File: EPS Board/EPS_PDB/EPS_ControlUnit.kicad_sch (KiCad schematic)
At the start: 42 parts, among them J6 Conn_01x04_Pin, J7 USB_B_Micro, SW1 SW_SPDT, U1 AMS1117-3.3, U2 TPS3824-33QDBVRQ1, U3 STM32L476VET6, Y1 32MHz

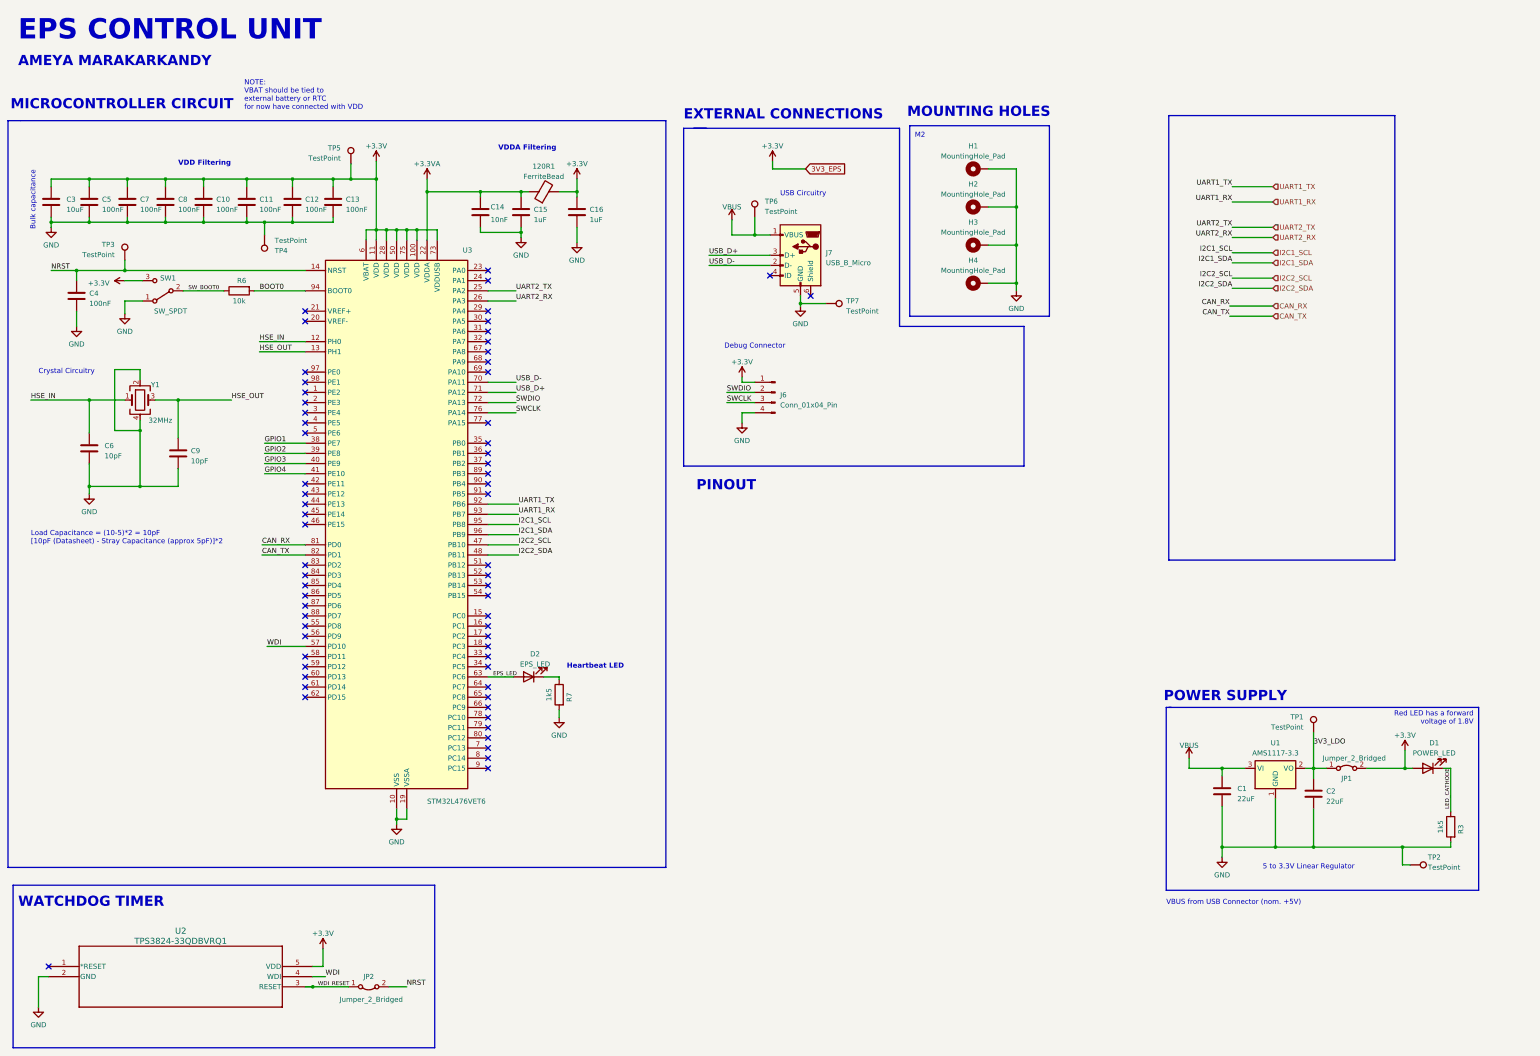
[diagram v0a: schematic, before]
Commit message: Modification of interfaces of EPS Control unit
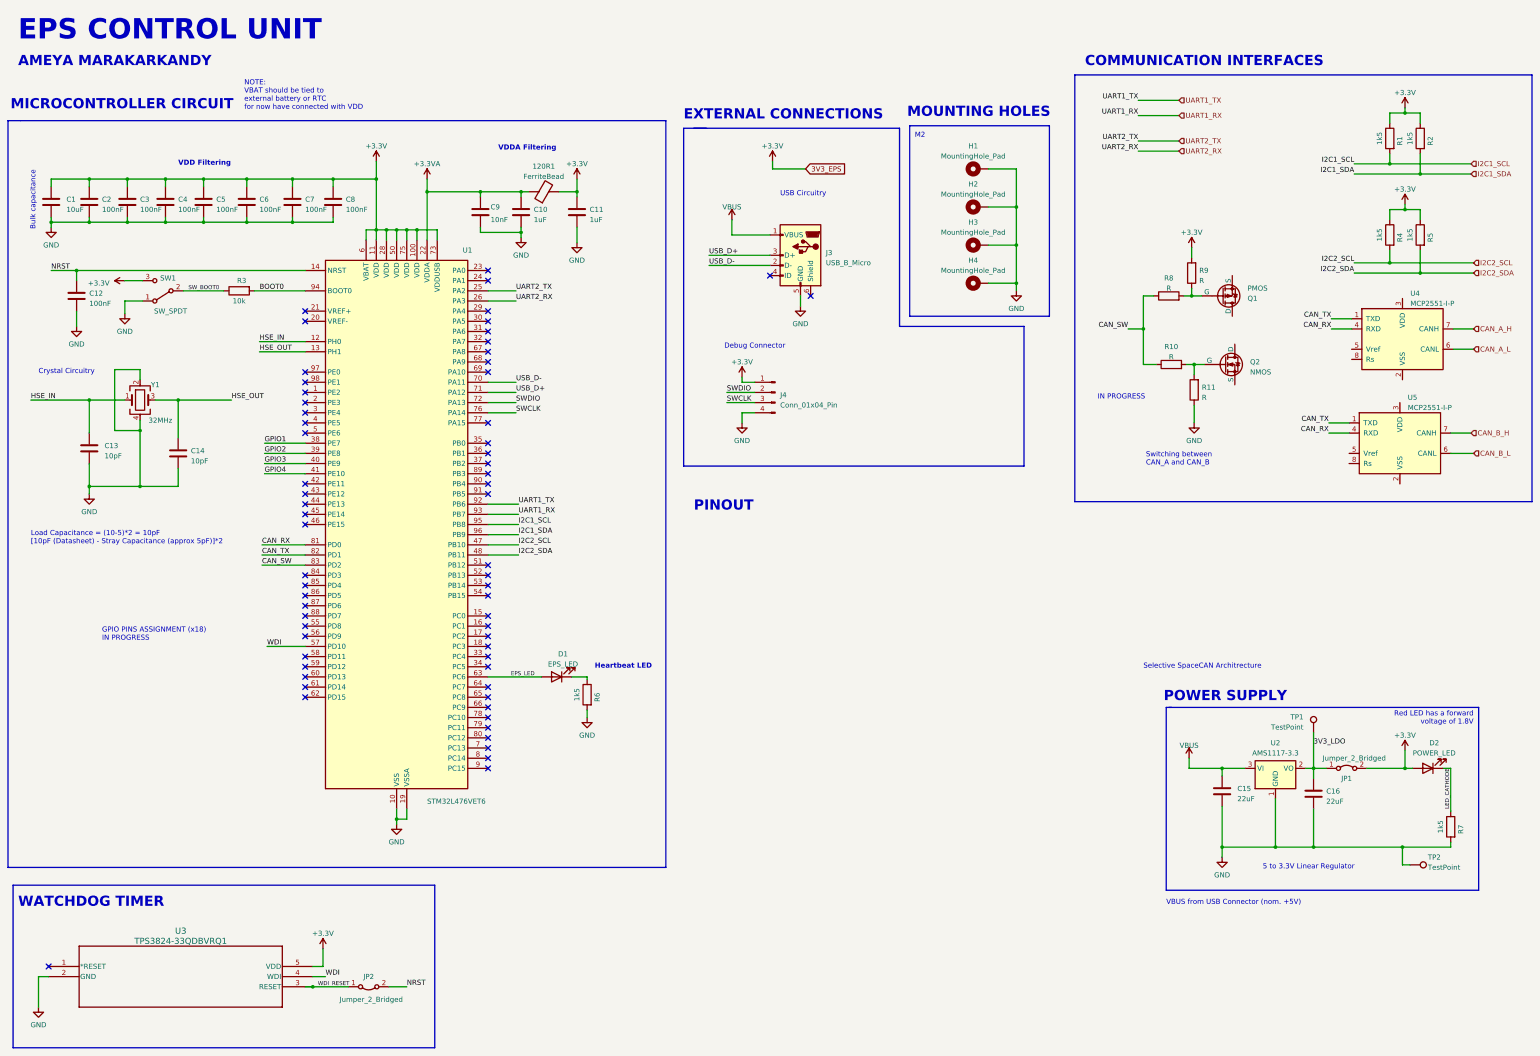
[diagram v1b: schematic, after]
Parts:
- removed TP3, TP4, TP5, TP6, TP7: TestPoint, symbol Connector:TestPoint
- added Q1: PMOS, symbol Simulation_SPICE:PMOS
- added Q2: NMOS, symbol Simulation_SPICE:NMOS
- added R1, R2, R4, R5: 1k5, symbol Device:R
- added R10, R11, R8, R9: R, symbol Device:R
- added U4, U5: MCP2551-I-P, Package_DIP:DIP-8_W7.62mm, symbol Interface_CAN_LIN:MCP2551-I-P
- renumbered C3 to C1, C15 to C10, C16 to C11, C4 to C12, C6 to C13, C9 to C14, C1 to C15, C2 to C16, C5 to C2, C7 to C3, C8 to C4, C10 to C5, C11 to C6, C12 to C7, C13 to C8, C14 to C9, D2 to D1, D1 to D2, J7 to J3, J6 to J4, R6 to R3, R7 to R6, R3 to R7, U3 to U1, U1 to U2, U2 to U3
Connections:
- net +3.3V: now also R1.1, R2.1, R4.1, R5.1, R9.2
- net CAN_RX: now also U4.4 (RXD), U5.4 (RXD)
- net CAN_TX: now also U4.1 (TXD), U5.1 (TXD)
- net GND: now also R11.1
- net I2C1_SCL: now also R1.2
- net I2C1_SDA: now also R2.2
- net I2C2_SCL: now also R4.2
- net I2C2_SDA: now also R5.2
- net CAN_SW: now reaches U1.83 (PD2)
- net CAN_SW: now also R10.1, R8.1
- new net: Q1.2 (G), R8.2, R9.1
- new net: Q2.2 (G), R10.2, R11.2
- new net CAN_A_H: U4.7 (CANH)
- new net CAN_A_L: U4.6 (CANL)
- new net CAN_B_H: U5.7 (CANH)
- new net CAN_B_L: U5.6 (CANL)
- no-connect marks 65 -> 64
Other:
- note added: "COMMUNICATION INTERFACES"
- note added: "GPIO PINS ASSIGNMENT (x18) IN PROGRESS"
- note added: "IN PROGRESS"
- note added: "Selective SpaceCAN Architrecture"
- note added: "Switching between CAN_A and CAN_B"
- moved on the sheet: D1, R6

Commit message: EPS PDB Board Schematic progress
Interfaces defined in EPS PDB board Schematic
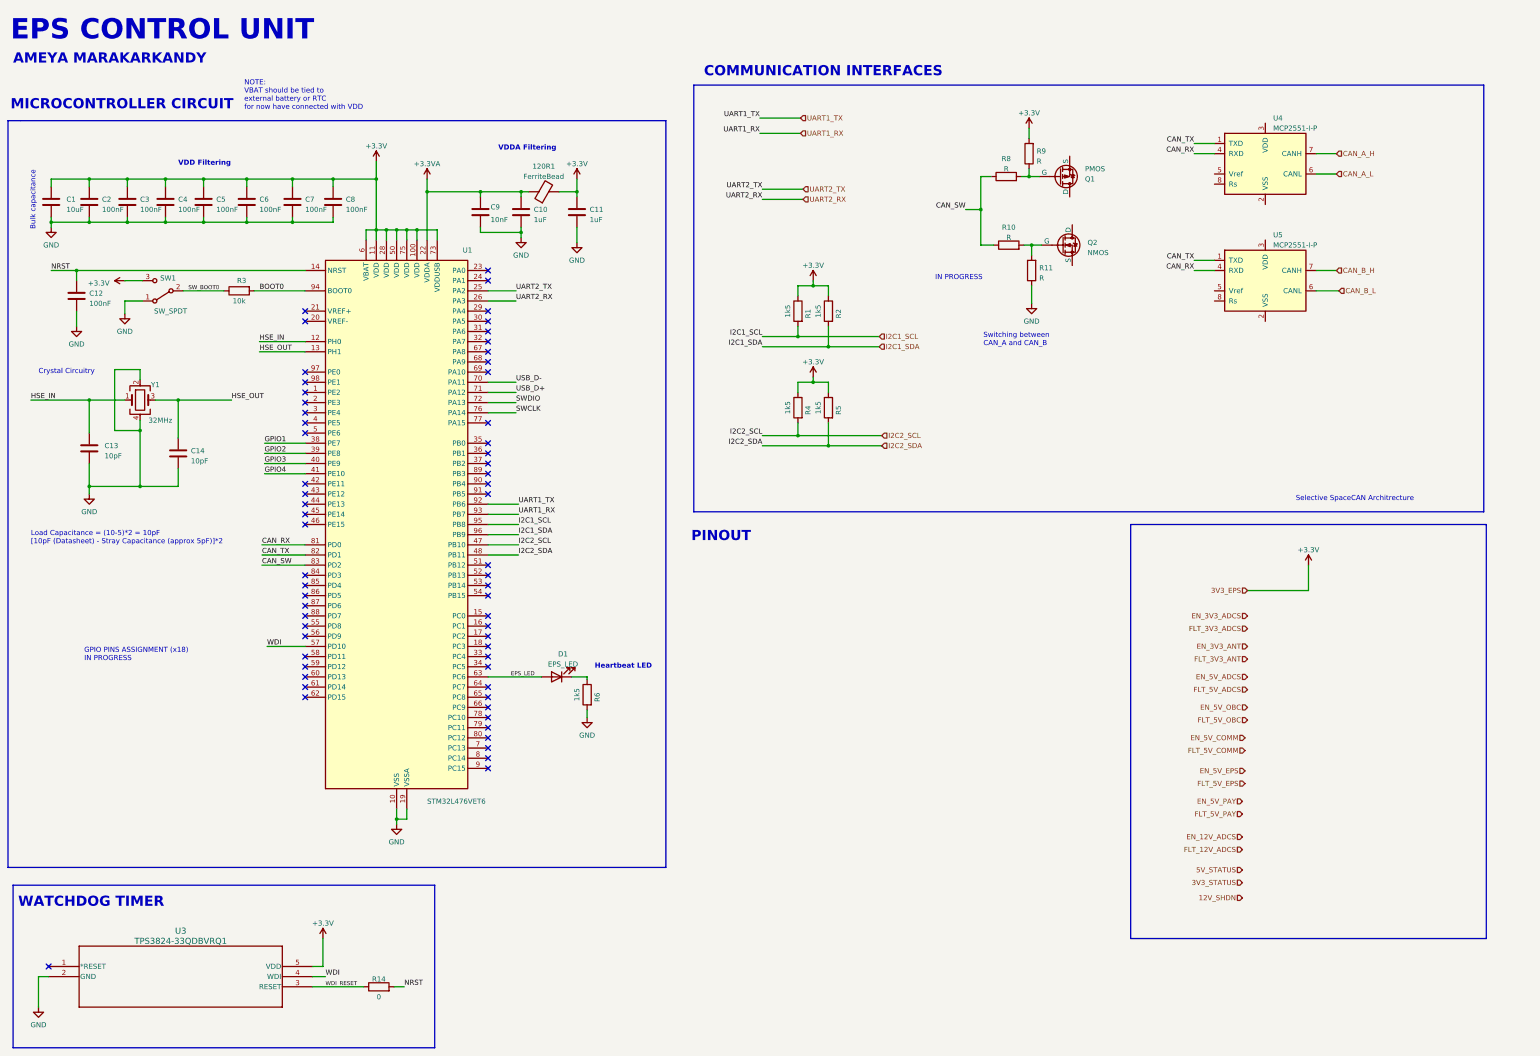
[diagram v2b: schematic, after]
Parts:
- removed C15, C16: 22uF, symbol Device:C
- removed D2: POWER_LED, symbol Device:LED
- removed H1, H2, H3, H4: MountingHole_Pad, symbol Mechanical:MountingHole_Pad
- removed J3: USB_B_Micro, symbol Connector:USB_B_Micro
- removed J4: Conn_01x04_Pin, symbol Connector:Conn_01x04_Pin
- removed JP1, JP2: Jumper_2_Bridged, symbol Jumper:Jumper_2_Bridged
- removed R7: 1k5, symbol Device:R
- removed TP1, TP2: TestPoint, symbol Connector:TestPoint
- removed U2: AMS1117-3.3, symbol Regulator_Linear:AMS1117-3.3
- added R14: 0, symbol Device:R
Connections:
- net NRST: now also R14.2
- net WDI_RESET: now also R14.1
- no-connect marks 64 -> 62
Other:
- note removed: "5 to 3.3V Linear Regulator"
- note removed: "Debug Connector"
- note removed: "EXTERNAL CONNECTIONS"
- note removed: "M2"
- note removed: "MOUNTING HOLES"
- note removed: "POWER SUPPLY"
- note removed: "Red LED has a forward voltage of 1.8V"
- note removed: "USB Circuitry"
- note removed: "VBUS from USB Connector (nom. +5V)"
- moved on the sheet: Q1, Q2, R1, R10, R11, R2, R4, R5, R8, R9, U4, U5

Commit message: EPS PDB Schematic Progress
Assigned STM32 GPIO pins
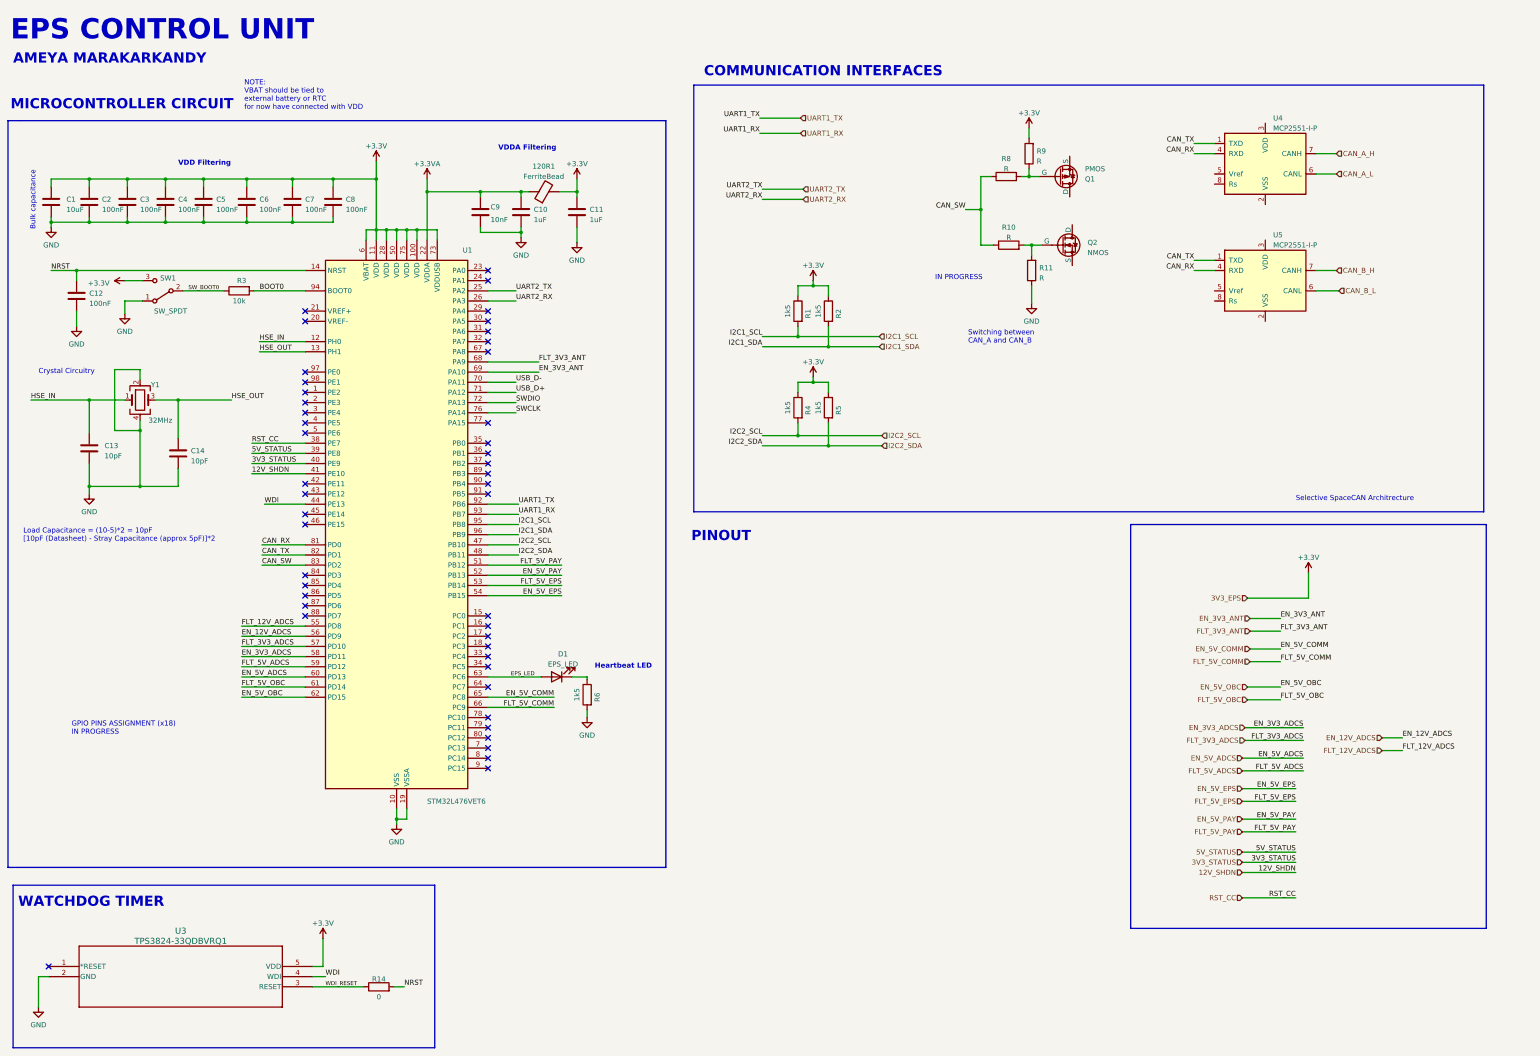
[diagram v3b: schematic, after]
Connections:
- net GPIO2 is gone; now on net 5V_STATUS: U1.39 (PE8)
- net GPIO3 is gone; now on net 3V3_STATUS: U1.40 (PE9)
- net GPIO4 is gone; now on net 12V_SHDN: U1.41 (PE10)
- net EN_12V_ADCS: now also U1.56 (PD9)
- net EN_3V3_ADCS: now also U1.58 (PD11)
- net EN_3V3_ANT: now also U1.69 (PA10)
- net EN_5V_ADCS: now also U1.60 (PD13)
- net EN_5V_COMM: now also U1.65 (PC8)
- net EN_5V_EPS: now also U1.54 (PB15)
- net EN_5V_OBC: now also U1.62 (PD15)
- net EN_5V_PAY: now also U1.52 (PB13)
- net FLT_12V_ADCS: now also U1.55 (PD8)
- net FLT_3V3_ADCS: now also U1.57 (PD10)
- net FLT_3V3_ANT: now also U1.68 (PA9)
- net FLT_5V_ADCS: now also U1.59 (PD12)
- net FLT_5V_COMM: now also U1.66 (PC9)
- net FLT_5V_EPS: now also U1.53 (PB14)
- net FLT_5V_OBC: now also U1.61 (PD14)
- net FLT_5V_PAY: now also U1.51 (PB12)
- net WDI: now also U1.44 (PE13); no longer U1.57 (PD10)
- net GPIO1 renamed RST_CC
- no-connect marks 62 -> 46

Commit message: Added PCB dxf outline
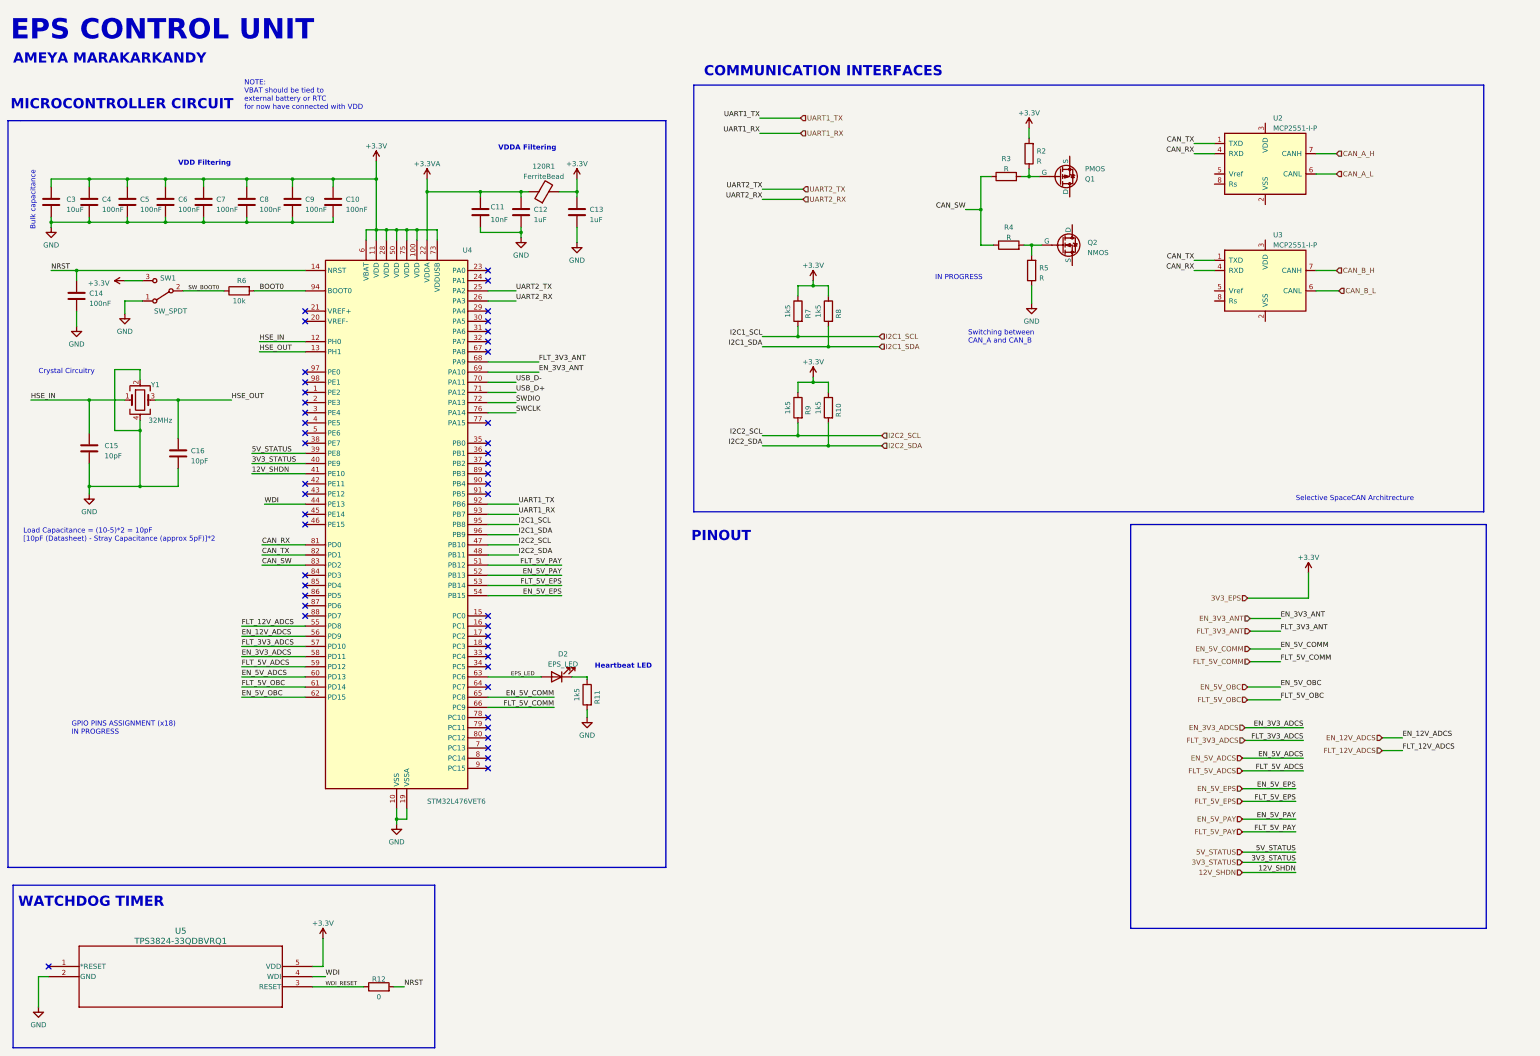
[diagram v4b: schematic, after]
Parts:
- renumbered C8 to C10, C9 to C11, C10 to C12, C11 to C13, C12 to C14, C13 to C15, C14 to C16, C1 to C3, C2 to C4, C3 to C5, C4 to C6, C5 to C7, C6 to C8, C7 to C9, D1 to D2, R5 to R10, R6 to R11, R14 to R12, R9 to R2, R8 to R3, R10 to R4, R11 to R5, R3 to R6, R1 to R7, R2 to R8, R4 to R9, U4 to U2, U5 to U3, U1 to U4, U3 to U5
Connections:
- net RST_CC: no longer names the net of U4.38 (PE7)
- no-connect marks 46 -> 47
